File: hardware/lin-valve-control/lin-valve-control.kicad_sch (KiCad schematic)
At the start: 40 parts, among them J1 QWIIC Connector, J2 Screw_Terminal_01x04, J3 DIN-5_180degree, J4 DIN-5_180degree, J5 Screw_Terminal_01x02, J6 Screw_Terminal_01x03, J7 Screw_Terminal_01x03, Q1 2N7002, Q2 2N7002, Q3 2N7002, Q4 2N7002, Q5 SUD50P04-08, Q6 SUD50P04-08, U1 Arduino_Nano_v3.x, U2 TJA1021T, U3 DRV8833PWP

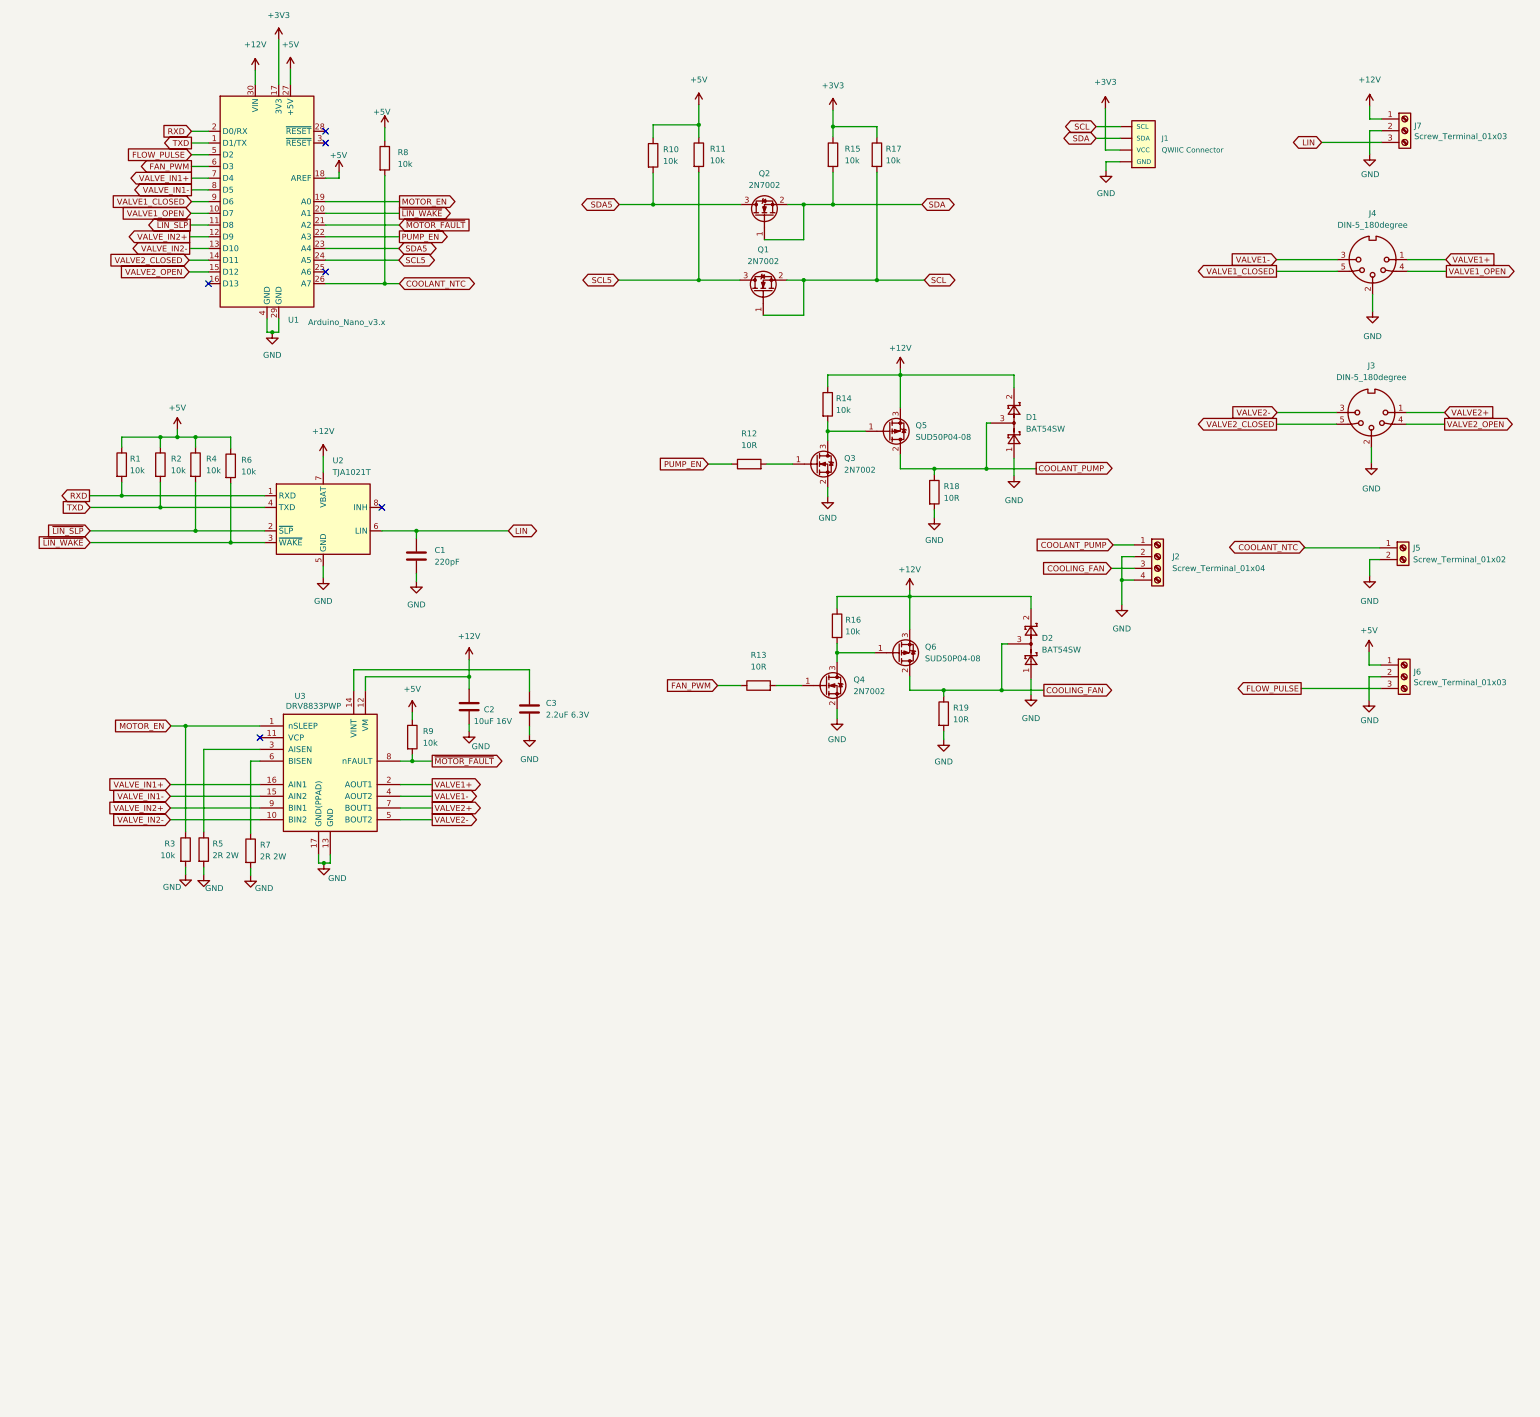
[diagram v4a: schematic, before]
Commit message: Splitting into multiple pages.
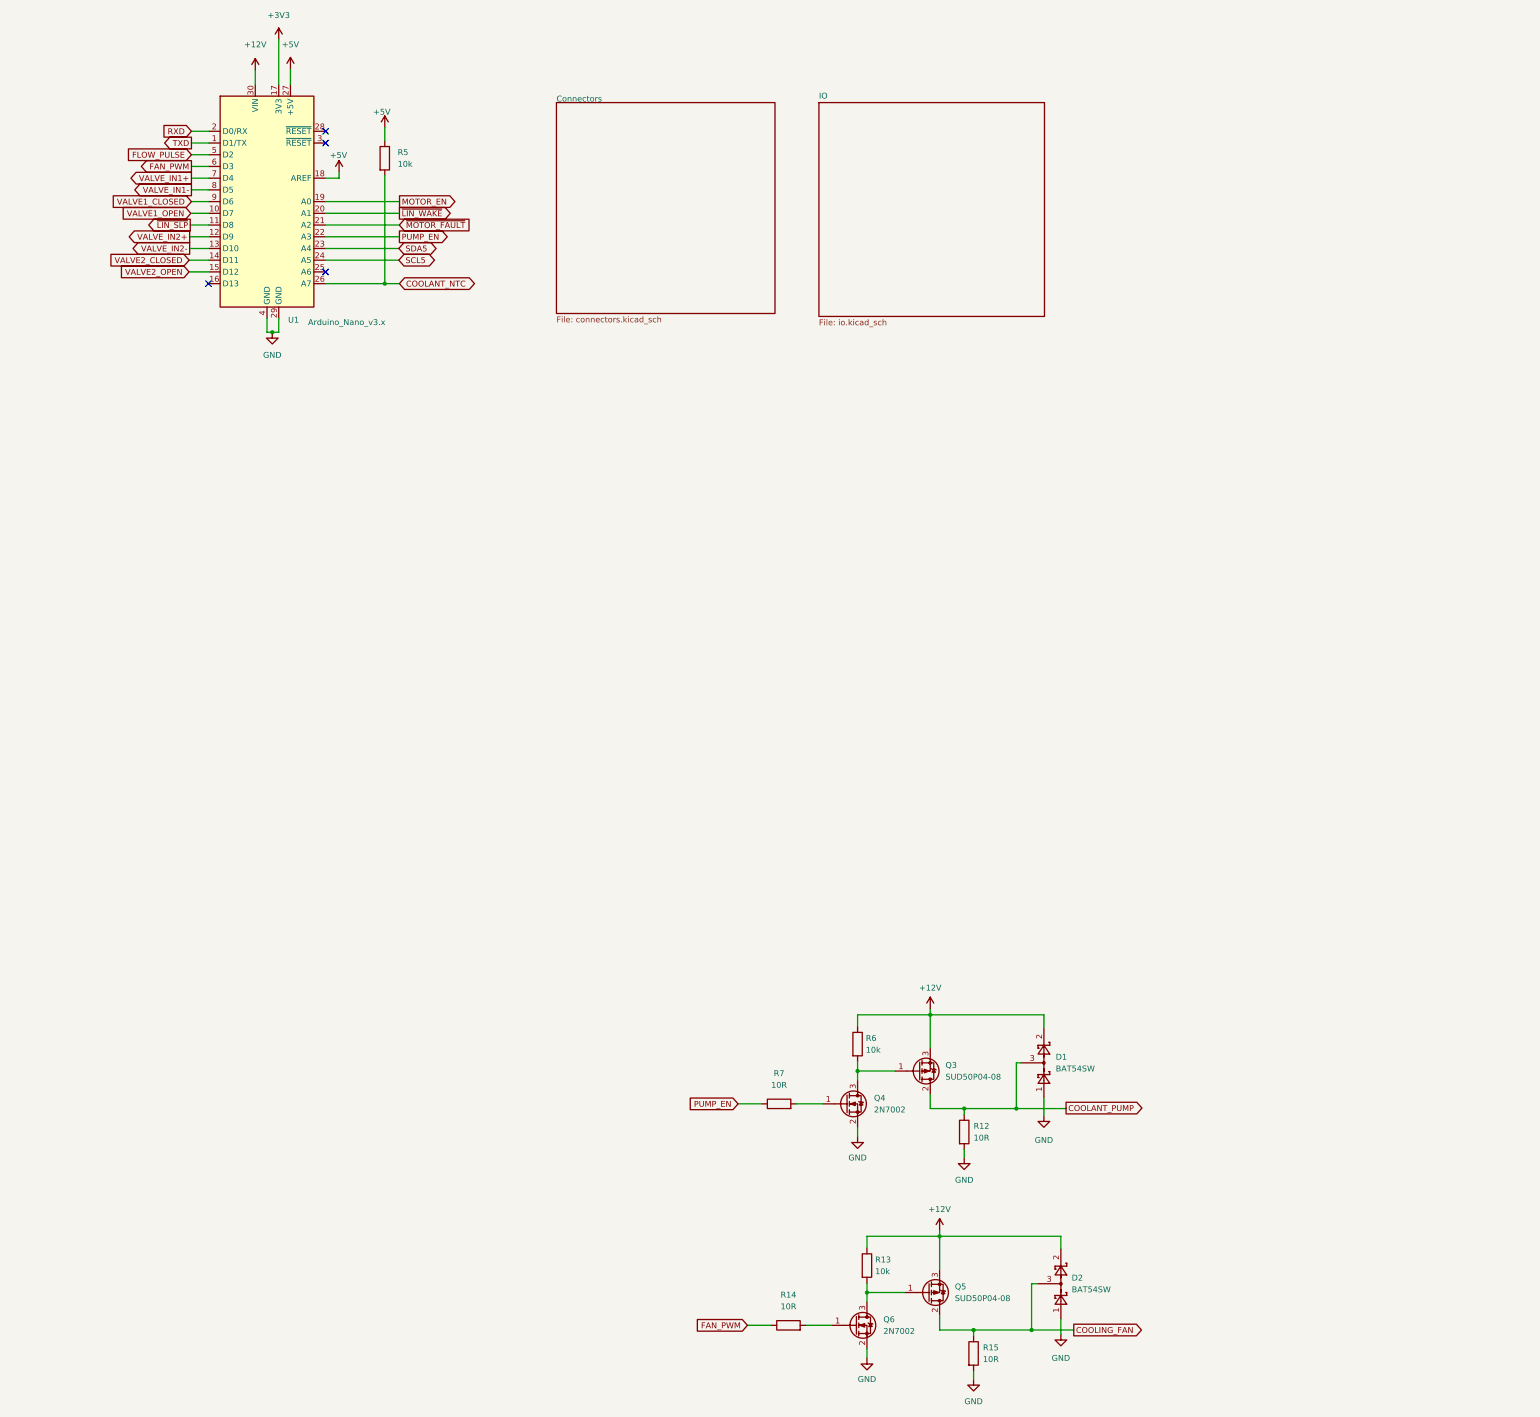
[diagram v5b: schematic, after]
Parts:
- removed C1: 220pF, Capacitor_SMD:C_0805_2012Metric_Pad1.18x1.45mm_HandSolder, symbol Device:C
- removed C2: 10uF 16V, Capacitor_SMD:C_1206_3216Metric_Pad1.33x1.80mm_HandSolder, symbol Device:C
- removed C3: 2.2uF 6.3V, Capacitor_SMD:C_1206_3216Metric_Pad1.33x1.80mm_HandSolder, symbol Device:C
- removed J1: QWIIC Connector, SparkFun-Connectors:1X04_1MM_RA, symbol SparkFun-Connectors:I2C_STANDARDQWIIC
- removed J2: Screw_Terminal_01x04, symbol Connector:Screw_Terminal_01x04
- removed J3, J4: DIN-5_180degree, SparkFun-Connectors:DIN5-RA-PTH, symbol Connector:DIN-5_180degree
- removed J5: Screw_Terminal_01x02, TerminalBlock_TE-Connectivity:TerminalBlock_TE_282834-2_1x02_P2.54mm_Horizontal, symbol Connector:Screw_Terminal_01x02
- removed J6, J7: Screw_Terminal_01x03, TerminalBlock_TE-Connectivity:TerminalBlock_TE_282834-3_1x03_P2.54mm_Horizontal, symbol Connector:Screw_Terminal_01x03
- removed Q1, Q2: 2N7002, Package_TO_SOT_SMD:SOT-23, symbol Transistor_FET:2N7002
- removed R1, R2, R3, R4, R6: 10k, Resistor_SMD:R_0805_2012Metric_Pad1.20x1.40mm_HandSolder, symbol Device:R
- removed R10, R11, R15, R17, R9: 10k, Resistor_SMD:R_0805_2012Metric, symbol Device:R
- removed R5, R7: 2R 2W, Resistor_SMD:R_2010_5025Metric_Pad1.40x2.65mm_HandSolder, symbol Device:R
- removed U2: TJA1021T, Package_SO:SOIC-8_3.9x4.9mm_P1.27mm, symbol Interface_CAN_LIN:TJA1021T
- removed U3: DRV8833PWP, Package_SO:HTSSOP-16-1EP_4.4x5mm_P0.65mm_EP3.4x5mm_Mask2.46x2.31mm_ThermalVias, symbol Driver_Motor:DRV8833PWP
- renumbered Q5 to Q3, Q3 to Q4, Q6 to Q5, Q4 to Q6, R18 to R12, R16 to R13, R13 to R14, R19 to R15, R8 to R5, R14 to R6, R12 to R7
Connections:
- no-connect marks 6 -> 4
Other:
- added sheet Connectors (connectors.kicad_sch)
- added sheet IO (io.kicad_sch)
- moved on the sheet: D1, D2, Q3, Q4, Q5, Q6, R12, R13, R14, R15, R6, R7

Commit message: Update lin-master firmware and valve control board
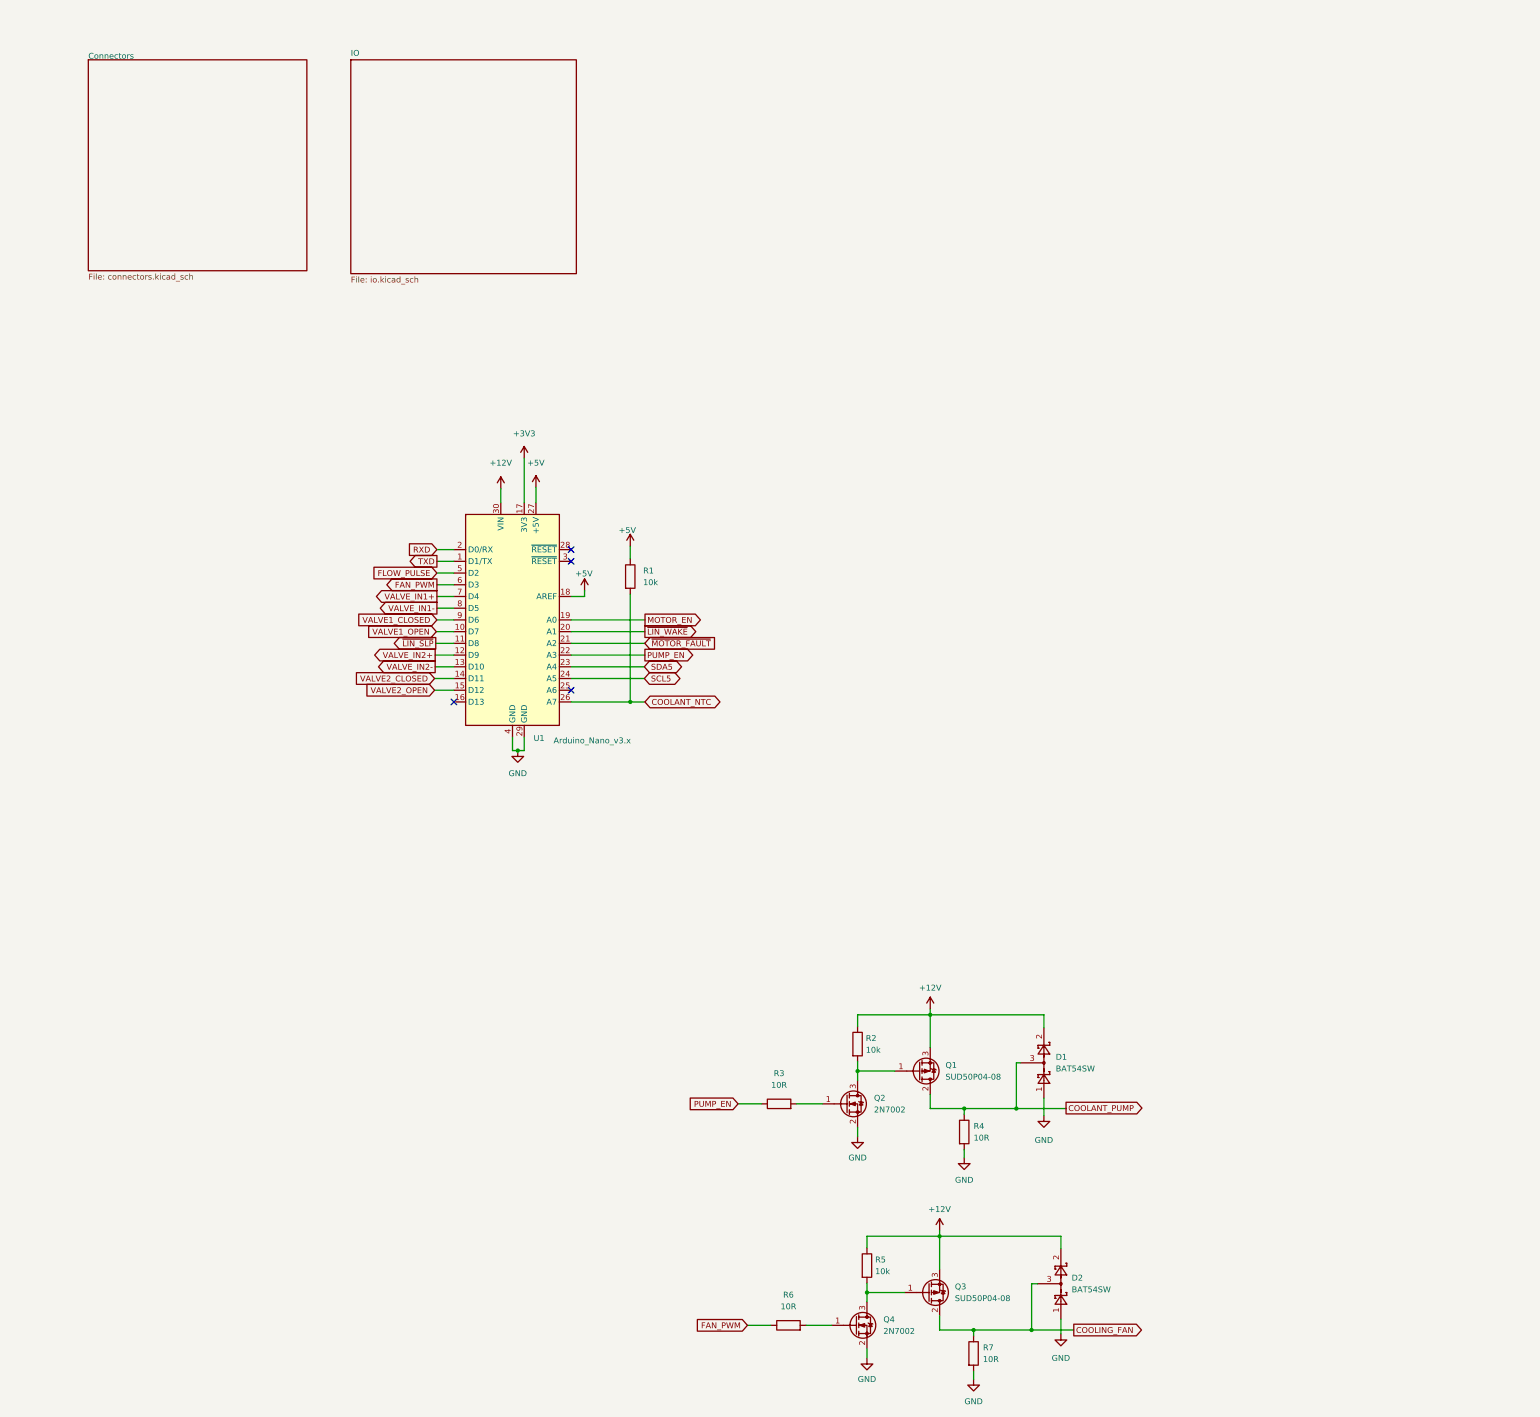
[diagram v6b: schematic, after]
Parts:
- R1: renamed from R5; footprint Resistor_SMD:R_0805_2012Metric -> Resistor_SMD:R_0805_2012Metric_Pad1.20x1.40mm_HandSolder
- renumbered Q3 to Q1, Q4 to Q2, Q5 to Q3, Q6 to Q4, R6 to R2, R7 to R3, R12 to R4, R13 to R5, R14 to R6, R15 to R7
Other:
- moved on the sheet: R1, U1
